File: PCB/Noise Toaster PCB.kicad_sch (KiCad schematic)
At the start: 0 parts

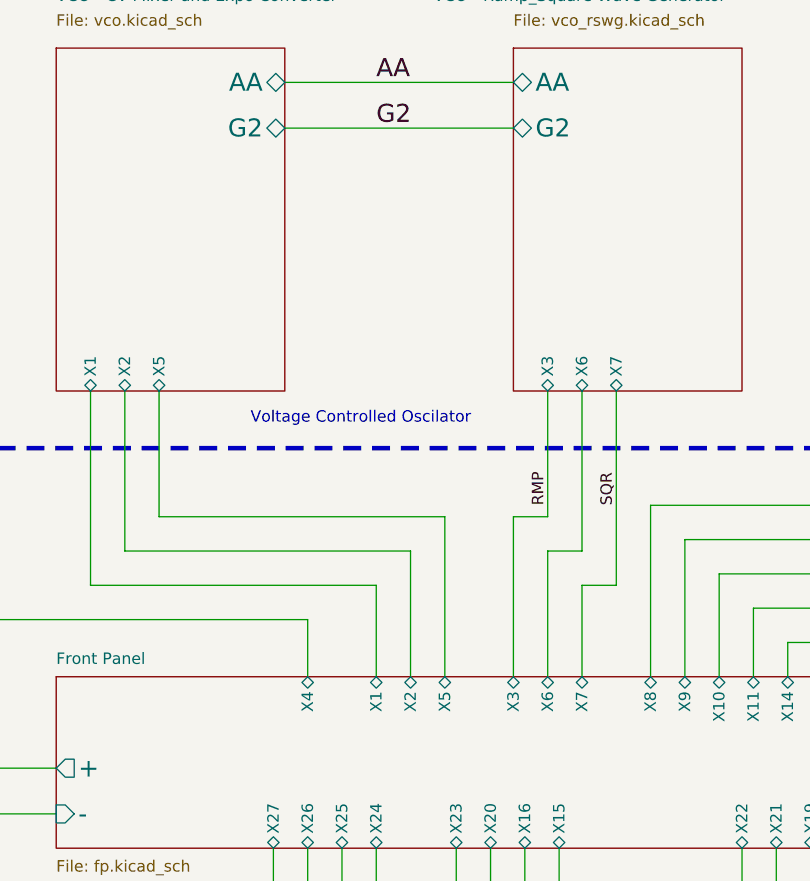
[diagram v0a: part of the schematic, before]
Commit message: Final Update
Move power pins closer to filter caps
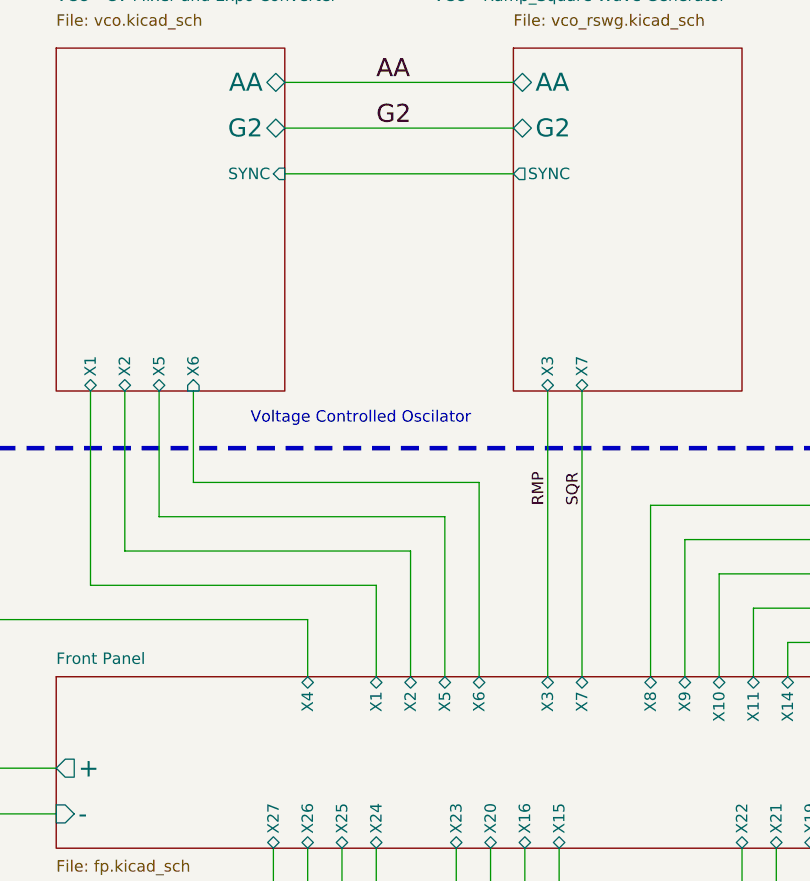
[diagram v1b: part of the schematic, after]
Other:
- sheet VCO - CV Mixer and Expo Converter ports: added SYNC, X6; removed none
- sheet VCO - Ramp_Square Wave Generator ports: added SYNC; removed X6
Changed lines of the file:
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@@
+	(wire
+		(pts
+			(xy 97.79 73.66) (xy 97.79 63.5)
+		)
+		(stroke
+			(width 0)
+			(type default)
+			(color 255 157 0 1)
+		)
+	)
 	(wire
 		(pts
@@
 	(wire
 		(pts
-			(xy 144.78 85.09) (xy 140.97 85.09)
-		)
-		(stroke
-			(width 0)
-			(type default)
-			(color 255 157 0 1)
-		)
-	)
-	(wire
-		(pts
 			(xy 170.18 114.3) (xy 170.18 129.54)
 		)
@@
 	(wire
 		(pts
-			(xy 144.78 63.5) (xy 144.78 85.09)
-		)
-		(stroke
-			(width 0)
-			(type default)
-			(color 255 157 0 1)
-		)
-	)
-	(wire
-		(pts
 			(xy 134.62 143.51) (xy 93.98 143.51)
 		)
@@
 	(wire
 		(pts
-			(xy 137.16 81.28) (xy 137.16 95.25)
-		)
-		(stroke
-			(width 0)
-			(type default)
-			(color 255 157 0 1)
-		)
-	)
-	(wire
-		(pts
 			(xy 241.3 142.24) (xy 266.7 142.24)
 		)
@@
 	(wire
 		(pts
-			(xy 137.16 77.47) (xy 133.35 77.47)
-		)
-		(stroke
-			(width 0)
-			(type default)
-			(color 255 157 0 1)
-		)
-	)
-	(wire
-		(pts
 			(xy 43.18 128.27) (xy 43.18 152.4)
 		)
@@
 	(wire
 		(pts
-			(xy 140.97 81.28) (xy 137.16 81.28)
-		)
-		(stroke
-			(width 0)
-			(type default)
-			(color 255 157 0 1)
-		)
-	)
-	(wire
-		(pts
 			(xy 110.49 88.9) (xy 110.49 95.25)
 		)
@@
 	(wire
 		(pts
-			(xy 140.97 85.09) (xy 140.97 95.25)
+			(xy 129.54 73.66) (xy 129.54 95.25)
+		)
+		(stroke
+			(width 0)
+			(type default)
+			(color 255 157 0 1)
+		)
+	)
+	(wire
+		(pts
+			(xy 107.95 39.37) (xy 133.35 39.37)
+		)
+		(stroke
+			(width 0)
+			(type default)
+		)
+	)
+	(wire
+		(pts
+			(xy 140.97 63.5) (xy 140.97 95.25)
 		)
 		(stroke
@@
 	(wire
 		(pts
-			(xy 137.16 63.5) (xy 137.16 77.47)
+			(xy 137.16 63.5) (xy 137.16 95.25)
 		)
 		(stroke
@@
 	(wire
 		(pts
+			(xy 129.54 73.66) (xy 97.79 73.66)
+		)
+		(stroke
+			(width 0)
+			(type default)
+			(color 255 157 0 1)
+		)
+	)
+	(wire
+		(pts
 			(xy 121.92 81.28) (xy 121.92 95.25)
 		)
@@
 	(wire
 		(pts
-			(xy 133.35 77.47) (xy 133.35 95.25)
-		)
-		(stroke
-			(width 0)
-			(type default)
-			(color 255 157 0 1)
-		)
-	)
-	(wire
-		(pts
 			(xy 198.12 80.01) (xy 152.4 80.01)
-		)
-		(stroke
-			(width 0)
-			(type default)
-			(color 255 157 0 1)
-		)
-	)
-	(wire
-		(pts
-			(xy 140.97 63.5) (xy 140.97 81.28)
 		)
 		(stroke
@@
 	)
 	(label "SQR"
-		(at 144.78 76.2 90)
+		(at 140.97 76.2 90)
 		(effects
 			(font
@@
 		)
 		(pin "X6" bidirectional
-			(at 137.16 95.25 90)
+			(at 129.54 95.25 90)
 			(effects
 				(font
@@
 		)
 		(pin "X3" bidirectional
-			(at 133.35 95.25 90)
+			(at 137.16 95.25 90)
 			(effects
 				(font
@@
 		)
 		(pin "X7" bidirectional
-			(at 144.78 63.5 270)
-			(effects
-				(font
-					(size 1.27 1.27)
-				)
-				(justify left)
-			)
-		)
-		(pin "X6" bidirectional
 			(at 140.97 63.5 270)
+			(effects
+				(font
+					(size 1.27 1.27)
+				)
+				(justify left)
+			)
+		)
+		(pin "SYNC" output
+			(at 133.35 39.37 180)
 			(effects
 				(font
@@
 			)
 		)
+		(pin "X6" input
+			(at 97.79 63.5 270)
+			(effects
+				(font
+					(size 1.27 1.27)
+				)
+				(justify left)
+			)
+		)
+		(pin "SYNC" input
+			(at 107.95 39.37 0)
+			(effects
+				(font
+					(size 1.27 1.27)
+				)
+				(justify right)
+			)
+		)
